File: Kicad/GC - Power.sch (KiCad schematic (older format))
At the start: 18 parts, among them U2 XC6220B331MR, U5 TPS54360DDA

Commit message: Fixed libraries issues
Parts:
- C3, C49, C50: footprint Capacitors_SMD:C_1206 -> Capacitor_SMD:C_1206_3216Metric; symbol Device:C -> Gouach_Controller-rescue:C-Device
- C46, C47, C51, C52, C53: footprint Capacitors_SMD:C_0603 -> Capacitor_SMD:C_0603_1608Metric; symbol Device:C -> Gouach_Controller-rescue:C-Device
- C48: footprint Romain:Capacitor_Horizontal -> Gouach-Controller:Capacitor_Horizontal; symbol Device:CP1 -> Gouach_Controller-rescue:CP1-Device
- C54: footprint Capacitors_SMD:CP_Elec_5x5.8 -> Capacitor_SMD:C_Elec_5x5.8; symbol Device:CP1 -> Gouach_Controller-rescue:CP1-Device
- D6: footprint Diodes_SMD:D_SOD-123F -> Diode_SMD:D_SOD-123F; symbol Device:D_Schottky -> Gouach_Controller-rescue:D_Schottky-Device
- L2: footprint Inductors_SMD:L_Coilcraft_XAL5030 -> Inductor_SMD:L_Coilcraft_XAL5030; symbol Device:L -> Gouach_Controller-rescue:L-Device
- R17, R44, R45, R5: footprint Resistors_SMD:R_0603 -> Resistor_SMD:R_0603_1608Metric; symbol Device:R -> Gouach_Controller-rescue:R-Device
- U2: footprint TO_SOT_Packages_SMD:SOT-23-5 -> Package_TO_SOT_SMD:SOT-23-5; symbol Regulator_Linear:XC6220B331MR -> Gouach_Controller-rescue:XC6220B331MR-Regulator_Linear
- U5: footprint Housings_SOIC:TI_SO-PowerPAD-8 -> Package_SO:TI_SO-PowerPAD-8; symbol Regulator_Switching:TPS54360DDA -> Gouach_Controller-rescue:TPS54360DDA-Regulator_Switching
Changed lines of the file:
@@
 $EndDescr
 $Comp
-L Device:C C?
+L Gouach_Controller-rescue:C-Device C?
 U 1 1 50500B3A
 P 6900 3950
@@
 F 0 "C46" H 7015 3996 50  0000 L CNN
 F 1 "10uF" H 7015 3905 50  0000 L CNN
-F 2 "Capacitors_SMD:C_0603" H 6900 3950 60  0001 C CNN
+F 2 "Capacitor_SMD:C_0603_1608Metric" H 6900 3950 60  0001 C CNN
 F 3 "" H 6900 3950 60  0001 C CNN
 F 4 "25V" H 6900 3950 50  0001 C CNN "Tension"
@@
 $EndComp
 $Comp
-L power:+3V3 #PWR0171
+L Gouach_Controller-rescue:+3V3-power #PWR0171
 U 1 1 5F178995
 P 6900 3650
@@
 $EndComp
 $Comp
-L power:+5V #PWR0172
+L Gouach_Controller-rescue:+5V-power #PWR0172
 U 1 1 5F179269
 P 5650 3650
@@
 $EndComp
 $Comp
-L power:GND #PWR0173
+L Gouach_Controller-rescue:GND-power #PWR0173
 U 1 1 5F17A322
 P 6350 4250
@@
 $EndComp
 $Comp
-L power:+5V #PWR0175
+L Gouach_Controller-rescue:+5V-power #PWR0175
 U 1 1 5F17B674
 P 1100 7050
@@
 $EndComp
 $Comp
-L power:PWR_FLAG #FLG0101
+L Gouach_Controller-rescue:PWR_FLAG-power #FLG0101
 U 1 1 5F17E894
 P 1100 7050
@@
 $EndComp
 $Comp
-L power:+BATT #PWR0177
+L Gouach_Controller-rescue:+BATT-power #PWR0177
 U 1 1 5F1803F2
 P 850 7050
@@
 $EndComp
 $Comp
-L power:PWR_FLAG #FLG0104
+L Gouach_Controller-rescue:PWR_FLAG-power #FLG0104
 U 1 1 5F180DCF
 P 850 7050
@@
 $EndComp
 $Comp
-L power:PWR_FLAG #FLG0103
+L Gouach_Controller-rescue:PWR_FLAG-power #FLG0103
 U 1 1 5F17F61E
 P 1850 7050
@@
 $EndComp
 $Comp
-L power:GND #PWR0174
+L Gouach_Controller-rescue:GND-power #PWR0174
 U 1 1 5F17B34C
 P 1850 7050
@@
 $EndComp
 $Comp
-L power:+3V3 #PWR0110
+L Gouach_Controller-rescue:+3V3-power #PWR0110
 U 1 1 5F59F4EE
 P 1600 7050
@@
 $EndComp
 $Comp
-L power:PWR_FLAG #FLG0102
+L Gouach_Controller-rescue:PWR_FLAG-power #FLG0102
 U 1 1 5F5A0DF0
 P 1600 7050
@@
 $EndComp
 $Comp
-L power:+BATT #PWR0131
+L Gouach_Controller-rescue:+BATT-power #PWR0131
 U 1 1 5E419F9F
 P 3550 4800
@@
 $EndComp
 $Comp
-L power:GND #PWR0176
+L Gouach_Controller-rescue:GND-power #PWR0176
 U 1 1 5E41A303
 P 3550 5100
@@
 $EndComp
 $Comp
-L Device:CP1 C48
+L Gouach_Controller-rescue:CP1-Device C48
 U 1 1 5E41B0CB
 P 3550 4950
 F 0 "C48" H 3665 4996 50  0000 L CNN
 F 1 "15uF" H 3665 4905 50  0000 L CNN
-F 2 "Romain:Capacitor_Horizontal" H 3550 4950 60  0001 C CNN
+F 2 "Gouach-Controller:Capacitor_Horizontal" H 3550 4950 60  0001 C CNN
 F 3 "" H 3550 4950 60  0001 C CNN
 F 4 "100V" H 3550 4950 50  0001 C CNN "Tension"
@@
 $EndComp
 $Comp
-L Device:C C?
+L Gouach_Controller-rescue:C-Device C?
 U 1 1 5E3F1C99
 P 5150 2150
@@
 F 0 "C50" H 5000 2250 50  0000 L CNN
 F 1 "10uF" H 4950 2050 50  0000 L CNN
-F 2 "Capacitors_SMD:C_1206" H 5150 2150 60  0001 C CNN
+F 2 "Capacitor_SMD:C_1206_3216Metric" H 5150 2150 60  0001 C CNN
 F 3 "" H 5150 2150 60  0001 C CNN
 F 4 "100V" H 5150 2150 50  0001 C CNN "Tension"
@@
 $EndComp
 $Comp
-L Device:C C?
+L Gouach_Controller-rescue:C-Device C?
 U 1 1 5E3F272D
 P 4850 2150
@@
 F 0 "C49" H 4700 2250 50  0000 L CNN
 F 1 "10uF" H 4650 2050 50  0000 L CNN
-F 2 "Capacitors_SMD:C_1206" H 4850 2150 60  0001 C CNN
+F 2 "Capacitor_SMD:C_1206_3216Metric" H 4850 2150 60  0001 C CNN
 F 3 "" H 4850 2150 60  0001 C CNN
 F 4 "100V" H 4850 2150 50  0001 C CNN "Tension"
@@
 $EndComp
 $Comp
-L Device:C C?
+L Gouach_Controller-rescue:C-Device C?
 U 1 1 5E3F2D18
 P 4550 2150
@@
 F 0 "C3" H 4450 2250 50  0000 L CNN
 F 1 "10uF" H 4350 2050 50  0000 L CNN
-F 2 "Capacitors_SMD:C_1206" H 4550 2150 60  0001 C CNN
+F 2 "Capacitor_SMD:C_1206_3216Metric" H 4550 2150 60  0001 C CNN
 F 3 "" H 4550 2150 60  0001 C CNN
 F 4 "100V" H 4550 2150 50  0001 C CNN "Tension"
@@
 $EndComp
 $Comp
-L Device:C C?
+L Gouach_Controller-rescue:C-Device C?
 U 1 1 5E3F2FBF
 P 7500 2300
@@
 F 0 "C52" H 7250 2350 50  0000 L CNN
 F 1 "51pF" H 7200 2250 50  0000 L CNN
-F 2 "Capacitors_SMD:C_0603" H 7500 2300 60  0001 C CNN
+F 2 "Capacitor_SMD:C_0603_1608Metric" H 7500 2300 60  0001 C CNN
 F 3 "" H 7500 2300 60  0001 C CNN
 F 4 "50V" H 7500 2300 50  0001 C CNN "Tension"
@@
 $EndComp
 $Comp
-L Device:C C?
+L Gouach_Controller-rescue:C-Device C?
 U 1 1 5E3F3459
 P 7800 2450
@@
 F 0 "C53" H 7915 2496 50  0000 L CNN
 F 1 "1.8nF" H 7915 2405 50  0000 L CNN
-F 2 "Capacitors_SMD:C_0603" H 7800 2450 60  0001 C CNN
+F 2 "Capacitor_SMD:C_0603_1608Metric" H 7800 2450 60  0001 C CNN
 F 3 "" H 7800 2450 60  0001 C CNN
 F 4 "50V" H 7800 2450 50  0001 C CNN "Tension"
@@
 $EndComp
 $Comp
-L Device:C C?
+L Gouach_Controller-rescue:C-Device C?
 U 1 1 5E3F36E9
 P 6650 1750
@@
 F 0 "C51" H 6700 1950 50  0000 L CNN
 F 1 "100nF" H 6700 1850 50  0000 L CNN
-F 2 "Capacitors_SMD:C_0603" H 6650 1750 60  0001 C CNN
+F 2 "Capacitor_SMD:C_0603_1608Metric" H 6650 1750 60  0001 C CNN
 F 3 "" H 6650 1750 60  0001 C CNN
 F 4 "50V" H 6650 1750 50  0001 C CNN "Tension"
@@
 $EndComp
 $Comp
-L Device:CP1 C54
+L Gouach_Controller-rescue:CP1-Device C54
 U 1 1 5E3F3DB2
 P 8100 2250
 F 0 "C54" H 8215 2296 50  0000 L CNN
 F 1 "68uF" H 8215 2205 50  0000 L CNN
-F 2 "Capacitors_SMD:CP_Elec_5x5.8" H 8100 2250 60  0001 C CNN
+F 2 "Capacitor_SMD:C_Elec_5x5.8" H 8100 2250 60  0001 C CNN
 F 3 "" H 8100 2250 60  0001 C CNN
 F 4 "10V" H 8100 2250 50  0001 C CNN "Tension"
@@
 $EndComp
 $Comp
-L Device:R R45
+L Gouach_Controller-rescue:R-Device R45
 U 1 1 5E3F4C7B
 P 7800 2150
 F 0 "R45" H 7730 2104 50  0000 R CNN
 F 1 "15.4k" H 7730 2195 50  0000 R CNN
-F 2 "Resistors_SMD:R_0603" V 7730 2150 50  0001 C CNN
+F 2 "Resistor_SMD:R_0603_1608Metric" V 7730 2150 50  0001 C CNN
 F 3 "" H 7800 2150 50  0001 C CNN
 	1    7800 2150
@@
 $EndComp
 $Comp
-L Device:R R5
+L Gouach_Controller-rescue:R-Device R5
 U 1 1 5E3F5DAA
 P 5450 2200
 F 0 "R5" H 5520 2246 50  0000 L CNN
 F 1 "274k" H 5520 2155 50  0000 L CNN
-F 2 "Resistors_SMD:R_0603" V 5380 2200 50  0001 C CNN
+F 2 "Resistor_SMD:R_0603_1608Metric" V 5380 2200 50  0001 C CNN
 F 3 "" H 5450 2200 50  0001 C CNN
 	1    5450 2200
@@
 $EndComp
 $Comp
-L Device:R R17
+L Gouach_Controller-rescue:R-Device R17
 U 1 1 5E3F6294
 P 7150 2100
 F 0 "R17" H 7220 2146 50  0000 L CNN
 F 1 "60.4k" H 7220 2055 50  0000 L CNN
-F 2 "Resistors_SMD:R_0603" V 7080 2100 50  0001 C CNN
+F 2 "Resistor_SMD:R_0603_1608Metric" V 7080 2100 50  0001 C CNN
 F 3 "" H 7150 2100 50  0001 C CNN
 	1    7150 2100
@@
 $EndComp
 $Comp
-L Device:R R44
+L Gouach_Controller-rescue:R-Device R44
 U 1 1 5E3F6705
 P 7150 2450
 F 0 "R44" H 7220 2496 50  0000 L CNN
 F 1 "11.5k" H 7220 2405 50  0000 L CNN
-F 2 "Resistors_SMD:R_0603" V 7080 2450 50  0001 C CNN
+F 2 "Resistor_SMD:R_0603_1608Metric" V 7080 2450 50  0001 C CNN
 F 3 "" H 7150 2450 50  0001 C CNN
 	1    7150 2450
@@
 $EndComp
 $Comp
-L Device:L L2
+L Gouach_Controller-rescue:L-Device L2
 U 1 1 5E3F69F6
 P 6900 1900
 F 0 "L2" V 7000 1900 50  0000 C CNN
 F 1 "10uH" V 6850 1900 50  0000 C CNN
-F 2 "Inductors_SMD:L_Coilcraft_XAL5030" H 6900 1900 50  0001 C CNN
+F 2 "Inductor_SMD:L_Coilcraft_XAL5030" H 6900 1900 50  0001 C CNN
 F 3 "XAL5050-103MEB" H 6900 1900 50  0001 C CNN
 F 4 "XAL5050-103MEB" H 6900 1900 50  0001 C CNN "mfg#"
@@
 $EndComp
 $Comp
-L Device:D_Schottky D6
+L Gouach_Controller-rescue:D_Schottky-Device D6
 U 1 1 5E3F81CC
 P 6700 2100
 F 0 "D6" V 6654 2179 50  0000 L CNN
 F 1 "60V" V 6745 2179 50  0000 L CNN
-F 2 "Diodes_SMD:D_SOD-123F" H 6700 2100 50  0001 C CNN
+F 2 "Diode_SMD:D_SOD-123F" H 6700 2100 50  0001 C CNN
 F 3 "PMEG6020ER-115" H 6700 2100 50  0001 C CNN
 F 4 "PMEG6020ER-115" H 6700 2100 50  0001 C CNN "mfg#"
@@
 	6550 2000 7500 2000
 $Comp
-L Regulator_Switching:TPS54360DDA U5
+L Gouach_Controller-rescue:TPS54360DDA-Regulator_Switching U5
 U 1 1 5E3E6755
 P 6150 1900
 F 0 "U5" H 6150 2367 50  0000 C CNN
 F 1 "TPS54360DDA" H 6150 2276 50  0000 C CNN
-F 2 "Housings_SOIC:TI_SO-PowerPAD-8" H 6200 1450 50  0001 L CIN
+F 2 "Package_SO:TI_SO-PowerPAD-8" H 6200 1450 50  0001 L CIN
 F 3 "http://www.ti.com/lit/ds/symlink/tps54360.pdf" H 6150 1900 50  0001 C CNN
 F 4 "TPS54360DDA" H 6150 1900 50  0001 C CNN "mfg#"
@@
 	6600 2300 7150 2300
 $Comp
-L power:VBUS #PWR09
+L Gouach_Controller-rescue:VBUS-power #PWR09
 U 1 1 5E434096
 P 8100 1850
@@
 Connection ~ 8100 1900
 $Comp
-L power:GND #PWR08
+L Gouach_Controller-rescue:GND-power #PWR08
 U 1 1 5E43659A
 P 6250 2700
@@
 $EndComp
 $Comp
-L power:+BATT #PWR07
+L Gouach_Controller-rescue:+BATT-power #PWR07
 U 1 1 5E436A14
 P 4550 1650
@@
 NoConn ~ 5750 2200
 $Comp
-L power:VBUS #PWR0106
+L Gouach_Controller-rescue:VBUS-power #PWR0106
 U 1 1 5E51FB26
 P 1350 7050
@@
 $EndComp
 $Comp
-L power:PWR_FLAG #FLG0105
+L Gouach_Controller-rescue:PWR_FLAG-power #FLG0105
 U 1 1 5E5211E0
 P 1350 7050
@@
 $EndComp
 $Comp
-L Regulator_Linear:XC6220B331MR U2
+L Gouach_Controller-rescue:XC6220B331MR-Regulator_Linear U2
 U 1 1 5E533A67
 P 6350 3800
 F 0 "U2" H 6350 4167 50  0000 C CNN
 F 1 "XC6220B331MR" H 6350 4076 50  0000 C CNN
-F 2 "TO_SOT_Packages_SMD:SOT-23-5" H 6350 3800 50  0001 C CNN
+F 2 "Package_TO_SOT_SMD:SOT-23-5" H 6350 3800 50  0001 C CNN
 F 3 "https://www.torexsemi.com/file/xc6220/XC6220.pdf" H 7100 2800 50  0001 C CNN
 	1    6350 3800
@@
 $EndComp
 $Comp
-L Device:C C?
+L Gouach_Controller-rescue:C-Device C?
 U 1 1 5E535C87
 P 5650 3950
@@
 F 0 "C47" H 5765 3996 50  0000 L CNN
 F 1 "10uF" H 5765 3905 50  0000 L CNN
-F 2 "Capacitors_SMD:C_0603" H 5650 3950 60  0001 C CNN
+F 2 "Capacitor_SMD:C_0603_1608Metric" H 5650 3950 60  0001 C CNN
 F 3 "" H 5650 3950 60  0001 C CNN
 F 4 "25V" H 5650 3950 50  0001 C CNN "Tension"

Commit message: Add Mouser order number
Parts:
- D6: Mouser (none) -> 771-PMEG6020ER-115; mfg# PMEG6020ER-115 -> (none)
- L2: Mouser (none) -> 994-XAL5050-103MEB; mfg# XAL5050-103MEB -> (none)
- U2: Mouser (none) -> 865-XC6220B331MR-G
- U5: Mouser (none) -> 595-TPS54360DDA; mfg# TPS54360DDA -> (none)
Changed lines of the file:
@@
 F 2 "Inductor_SMD:L_Coilcraft_XAL5030" H 6900 1900 50  0001 C CNN
 F 3 "XAL5050-103MEB" H 6900 1900 50  0001 C CNN
-F 4 "XAL5050-103MEB" H 6900 1900 50  0001 C CNN "mfg#"
+F 4 "" H 6900 1900 50  0001 C CNN "mfg#"
+F 5 "994-XAL5050-103MEB" H 6900 1900 50  0001 C CNN "Mouser"
 	1    6900 1900
 	0    -1   -1   0
@@
 F 1 "60V" V 6745 2179 50  0000 L CNN
 F 2 "Diode_SMD:D_SOD-123F" H 6700 2100 50  0001 C CNN
-F 3 "PMEG6020ER-115" H 6700 2100 50  0001 C CNN
-F 4 "PMEG6020ER-115" H 6700 2100 50  0001 C CNN "mfg#"
+F 3 "https://assets.nexperia.com/documents/data-sheet/PMEG6020ER.pdf" H 6700 2100 50  0001 C CNN
+F 4 "" H 6700 2100 50  0001 C CNN "mfg#"
+F 5 "771-PMEG6020ER-115" H 6700 2100 50  0001 C CNN "Mouser"
 	1    6700 2100
 	0    1    1    0
@@
 F 2 "Package_SO:TI_SO-PowerPAD-8" H 6200 1450 50  0001 L CIN
 F 3 "http://www.ti.com/lit/ds/symlink/tps54360.pdf" H 6150 1900 50  0001 C CNN
-F 4 "TPS54360DDA" H 6150 1900 50  0001 C CNN "mfg#"
+F 4 "" H 6150 1900 50  0001 C CNN "mfg#"
+F 5 "595-TPS54360DDA" H 6150 1900 50  0001 C CNN "Mouser"
 	1    6150 1900
 	1    0    0    -1
@@
 F 2 "Package_TO_SOT_SMD:SOT-23-5" H 6350 3800 50  0001 C CNN
 F 3 "https://www.torexsemi.com/file/xc6220/XC6220.pdf" H 7100 2800 50  0001 C CNN
+F 4 "" H 6350 3800 50  0001 C CNN "mfg#"
+F 5 "865-XC6220B331MR-G " H 6350 3800 50  0001 C CNN "Mouser"
 	1    6350 3800
 	1    0    0    -1

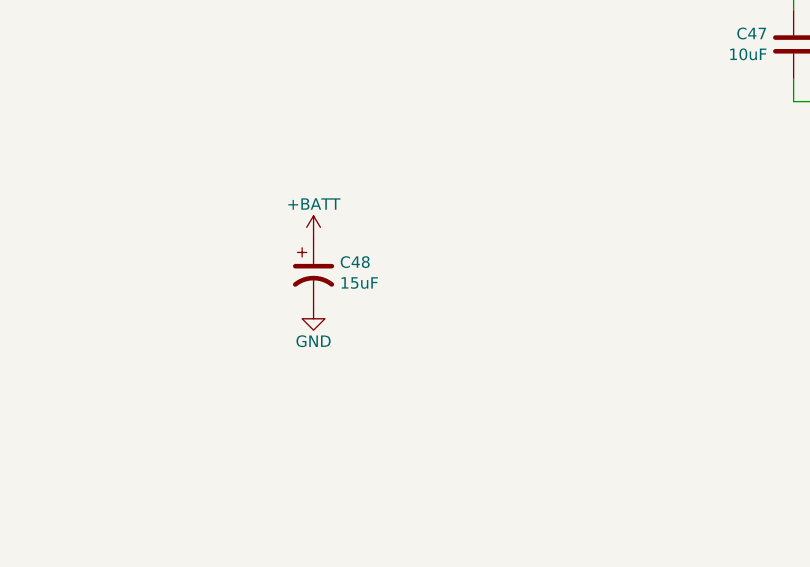
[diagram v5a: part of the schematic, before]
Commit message: Add capacitor ref
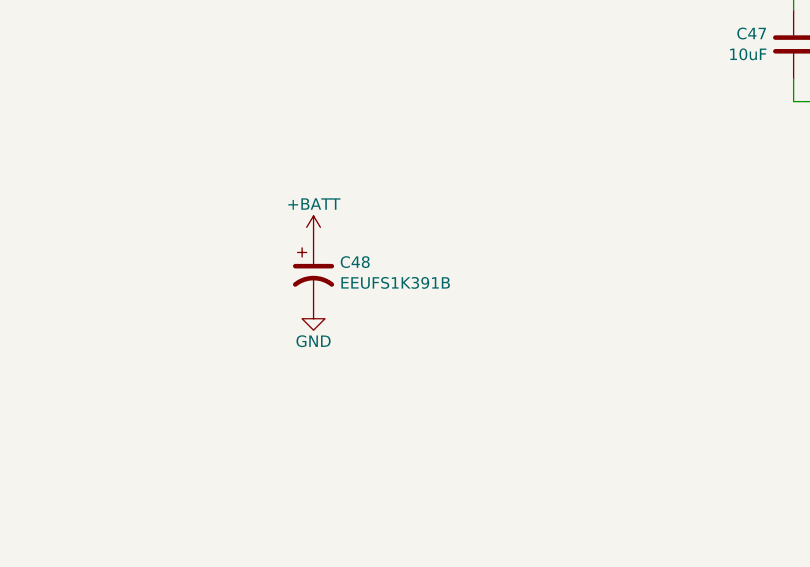
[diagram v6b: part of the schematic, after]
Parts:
- C48: value 15uF -> EEUFS1K391B
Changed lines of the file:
@@
 P 3550 4950
 F 0 "C48" H 3665 4996 50  0000 L CNN
-F 1 "15uF" H 3665 4905 50  0000 L CNN
+F 1 "EEUFS1K391B" H 3665 4905 50  0000 L CNN
 F 2 "Gouach-Controller:Capacitor_Horizontal" H 3550 4950 60  0001 C CNN
 F 3 "" H 3550 4950 60  0001 C CNN
